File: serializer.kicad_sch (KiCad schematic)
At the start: 1 part

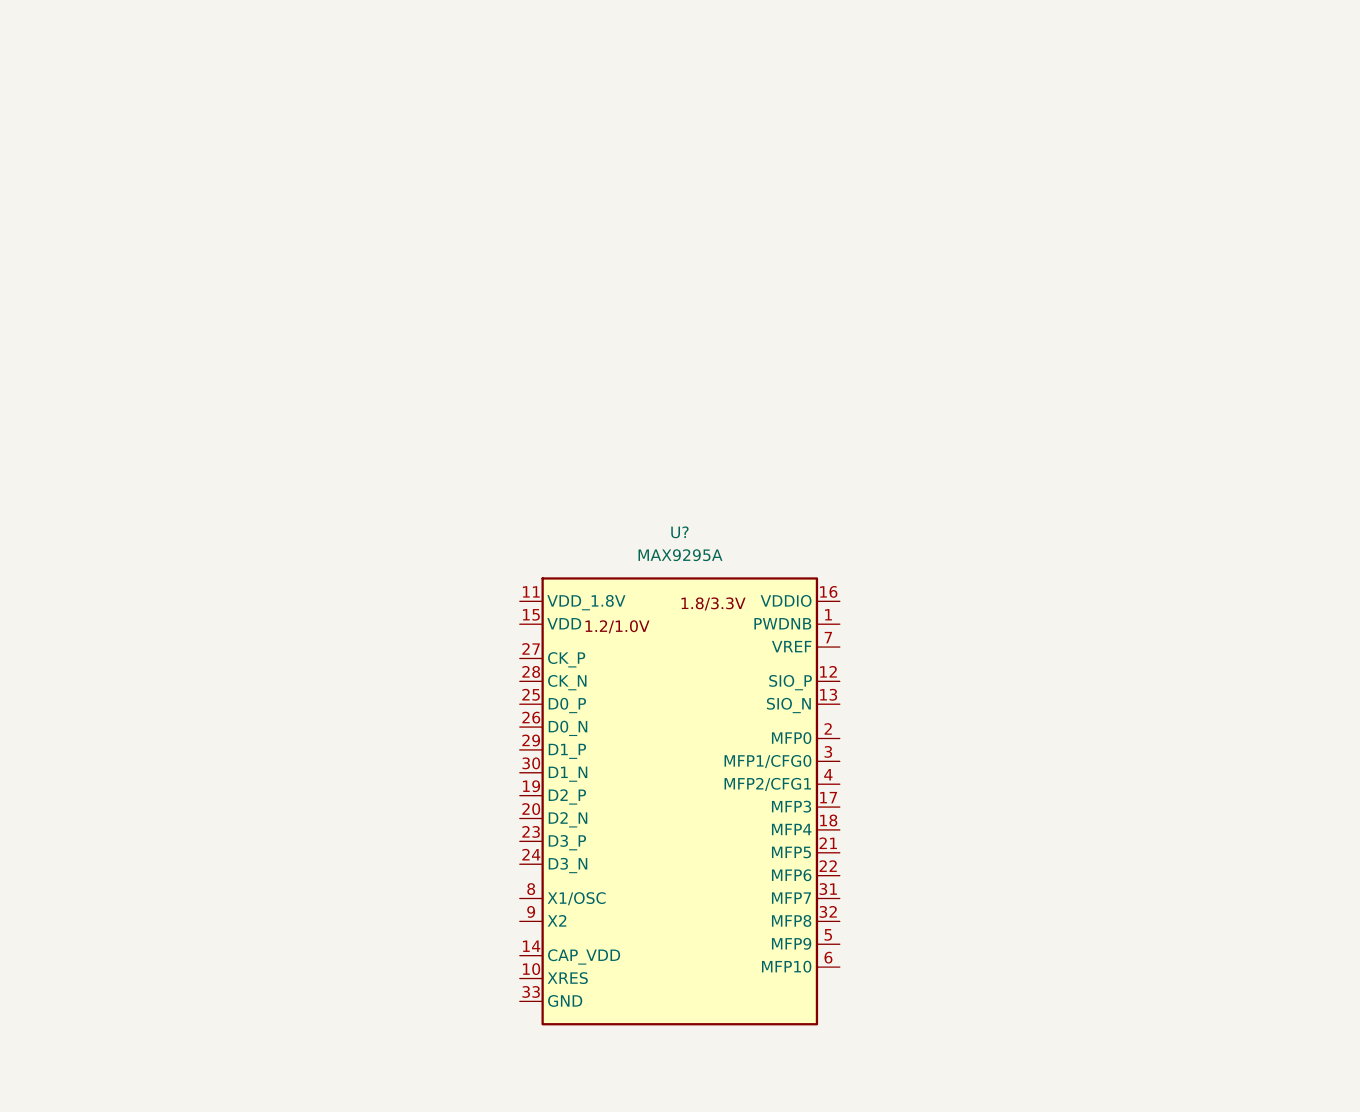
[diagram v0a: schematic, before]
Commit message: Add serializer supply filtration
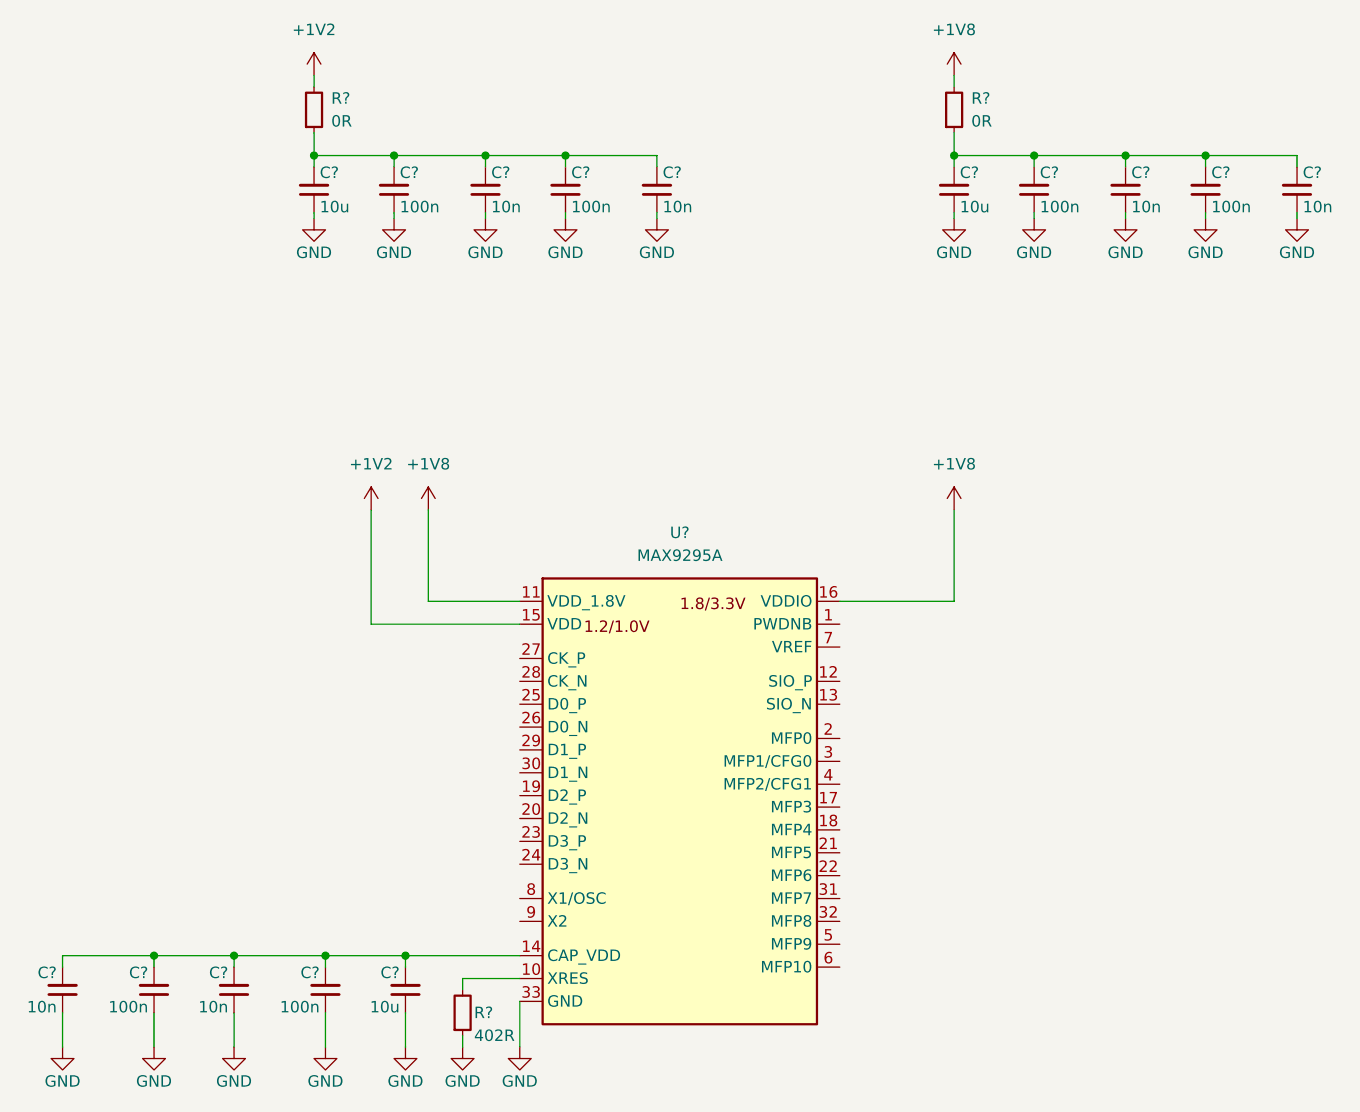
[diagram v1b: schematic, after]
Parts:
- added C? (x6): C_100n_0402, antmicro-footprints:C_0402_1005Metric, symbol antmicroCapacitors0402:C_100n_0402
- added C? (x6): C_10n_0402, antmicro-footprints:C_0402_1005Metric, symbol antmicroCapacitors0402:C_10n_0402
- added C? (x3): C_10u_0402, antmicro-footprints:C_0402_1005Metric, symbol antmicroCapacitors0402:C_10u_0402
- added R? (x2): R_0R_0402, antmicro-footprints:R_0402_1005Metric, symbol antmicroResistors0402:R_0R_0402
- added R?: R_402R_0402, antmicro-footprints:R_0402_1005Metric, symbol antmicroResistors0402:R_402R_0402
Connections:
- net at U?.10 (XRES): now also R?.2
- net +1V8: now reaches U?.11 (VDD_1.8V)
- net +1V8: now also U?.16 (VDDIO), R?.2
- net at U?.14 (CAP_VDD): now also C?.2, C?.2, C?.2, C?.2, C?.2
- net +1V2: now reaches U?.15 (VDD)
- net +1V2: now also R?.2
- net GND: now reaches U?.33 (GND)
- net GND: now also C?.1, C?.1, C?.1, C?.1, C?.1, C?.1, C?.1, C?.1, C?.1, C?.1, C?.1, C?.1, C?.1, C?.1, C?.1, R?.1
- new net: C?.2, C?.2, C?.2, C?.2, C?.2, R?.1 (x2)

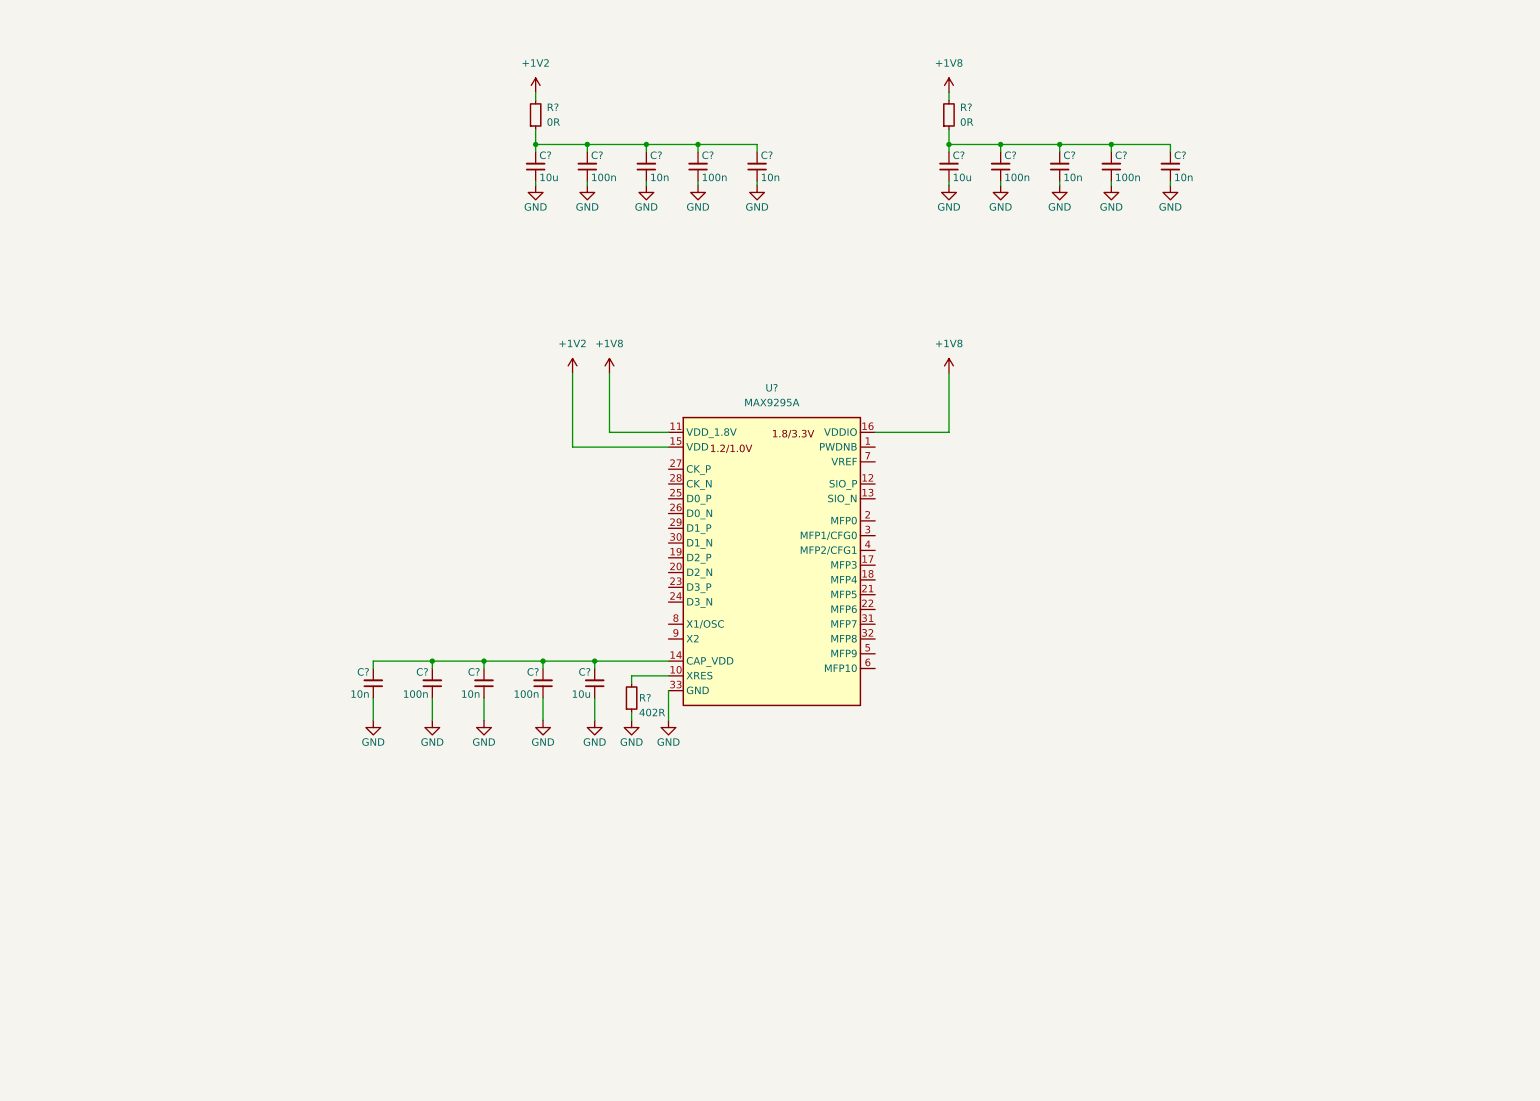
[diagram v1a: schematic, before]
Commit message: [WiP]:Add serializer signals and decoupling capacitors
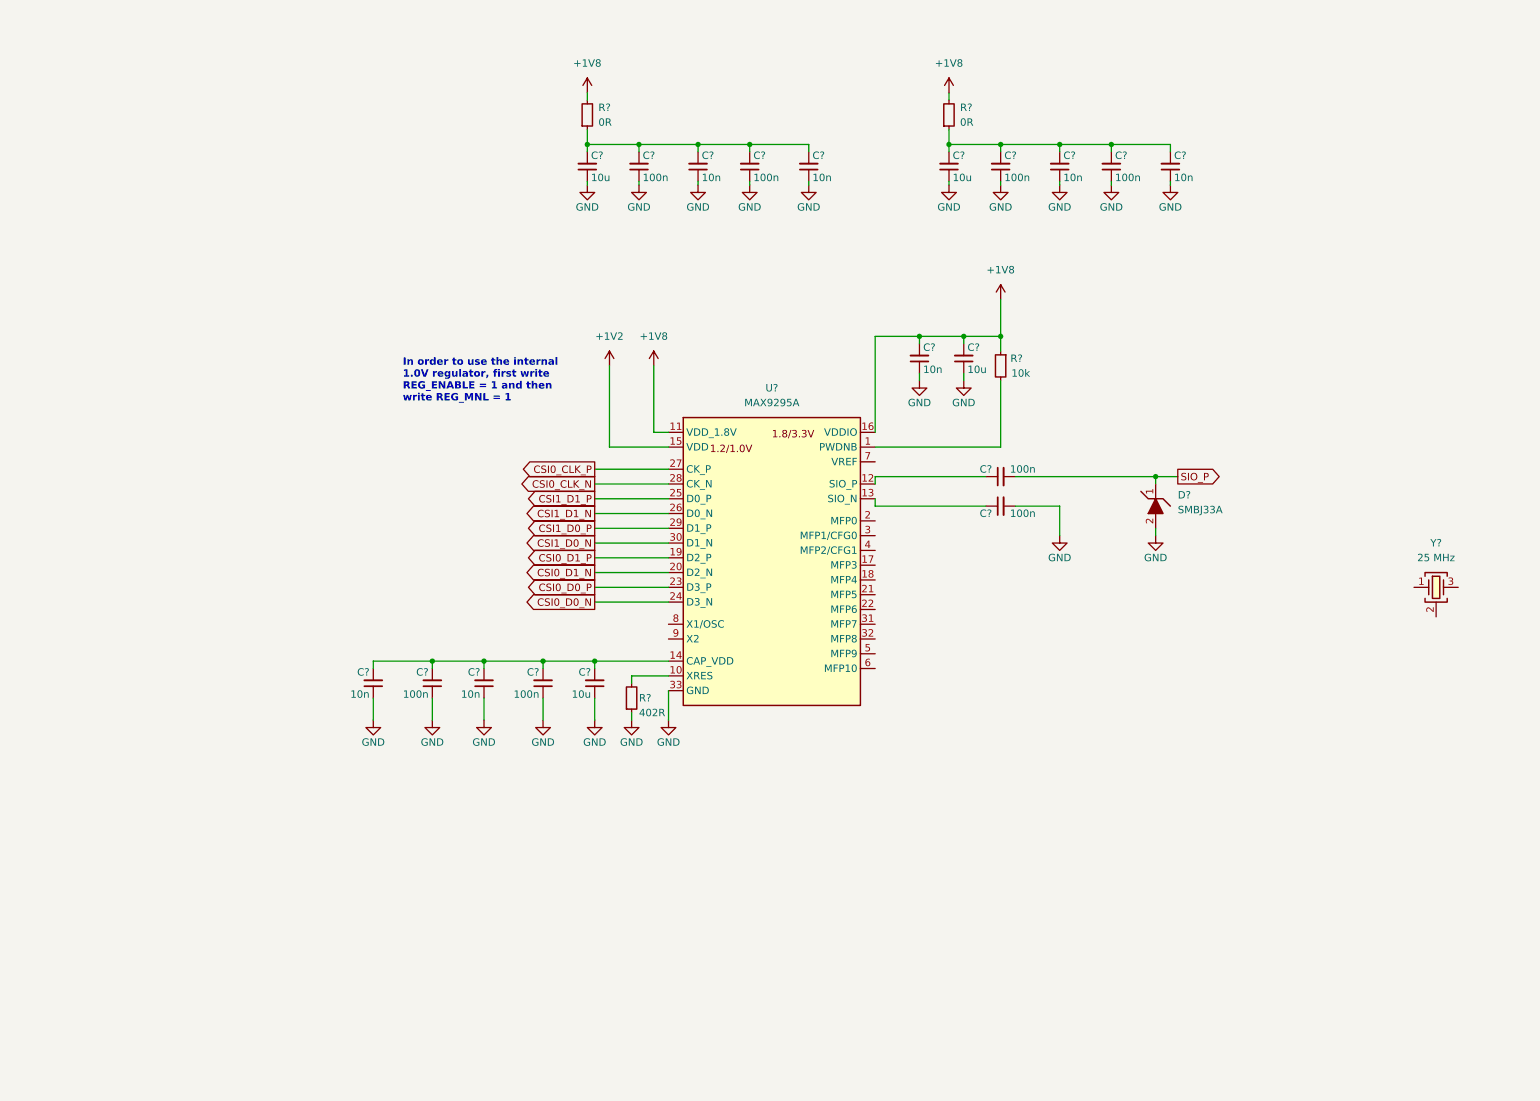
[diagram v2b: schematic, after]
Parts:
- removed C? (x2): C_10n_0402, antmicro-footprints:C_0402_1005Metric, symbol antmicroCapacitors0402:C_10n_0402
- removed C? (x2): C_100n_0402, antmicro-footprints:C_0402_1005Metric, symbol antmicroCapacitors0402:C_100n_0402
- removed C?: C_10u_0402, antmicro-footprints:C_0402_1005Metric, symbol antmicroCapacitors0402:C_10u_0402
- removed R?: R_0R_0402, antmicro-footprints:R_0402_1005Metric, symbol antmicroResistors0402:R_0R_0402
- added C? (x2): C_10u_0402, antmicro-footprints:C_0402_1005Metric, symbol antmicroCapacitors0402:C_10u_0402
- added C? (x4): C_100n_0402, antmicro-footprints:C_0402_1005Metric, symbol antmicroCapacitors0402:C_100n_0402
- added C? (x3): C_10n_0402, antmicro-footprints:C_0402_1005Metric, symbol antmicroCapacitors0402:C_10n_0402
- added D?: SMBJ33A, antmicro-footprints:D_SMB, symbol antmicroTVSDiodes:SMBJ33A
- added R?: R_0R_0402, antmicro-footprints:R_0402_1005Metric, symbol antmicroResistors0402:R_0R_0402
- added R?: R_10k_0402, antmicro-footprints:R_0402_1005Metric, symbol antmicroResistors0402:R_10k_0402
- added Y?: Resonator_25MHz_ABM8G, antmicro-footprints:Oscillator_SMD_Geyer_KX-7-4Pin_3.2x2.5mm, symbol antmicroResonators:Resonator_25MHz_ABM8G
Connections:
- net +1V8: now also C?.2, C?.2, R?.1, R?.2
- net GND: now also C?.1, C?.1, C?.1, C?.1, C?.1, C?.1, C?.1, C?.2, D?.2
- net at U?.1 (PWDNB): now also R?.2
- net at U?.12 (SIO_P): now also C?.1
- net at U?.13 (SIO_N): now also C?.1
- net CSI0_D1_P: now reaches U?.19 (D2_P)
- net CSI0_D1_N: now reaches U?.20 (D2_N)
- net CSI0_D0_P: now reaches U?.23 (D3_P)
- net CSI0_D0_N: now reaches U?.24 (D3_N)
- net CSI1_D1_P: now reaches U?.25 (D0_P)
- net CSI1_D1_N: now reaches U?.26 (D0_N)
- net CSI0_CLK_P: now reaches U?.27 (CK_P)
- net CSI0_CLK_N: now reaches U?.28 (CK_N)
- net CSI1_D0_P: now reaches U?.29 (D1_P)
- net CSI1_D0_N: now reaches U?.30 (D1_N)
- new net: C?.2, C?.2, C?.2, C?.2, C?.2, R?.1
- new net: Y?.2 (SH), Y?.4 (SH)
- new net SIO_P: C?.2, D?.1
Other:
- note added: "In order to use the internal 1.0V regulator, first write REG_ENABLE = 1 and then write REG_MNL = 1"

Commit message: Add cfg pins handling
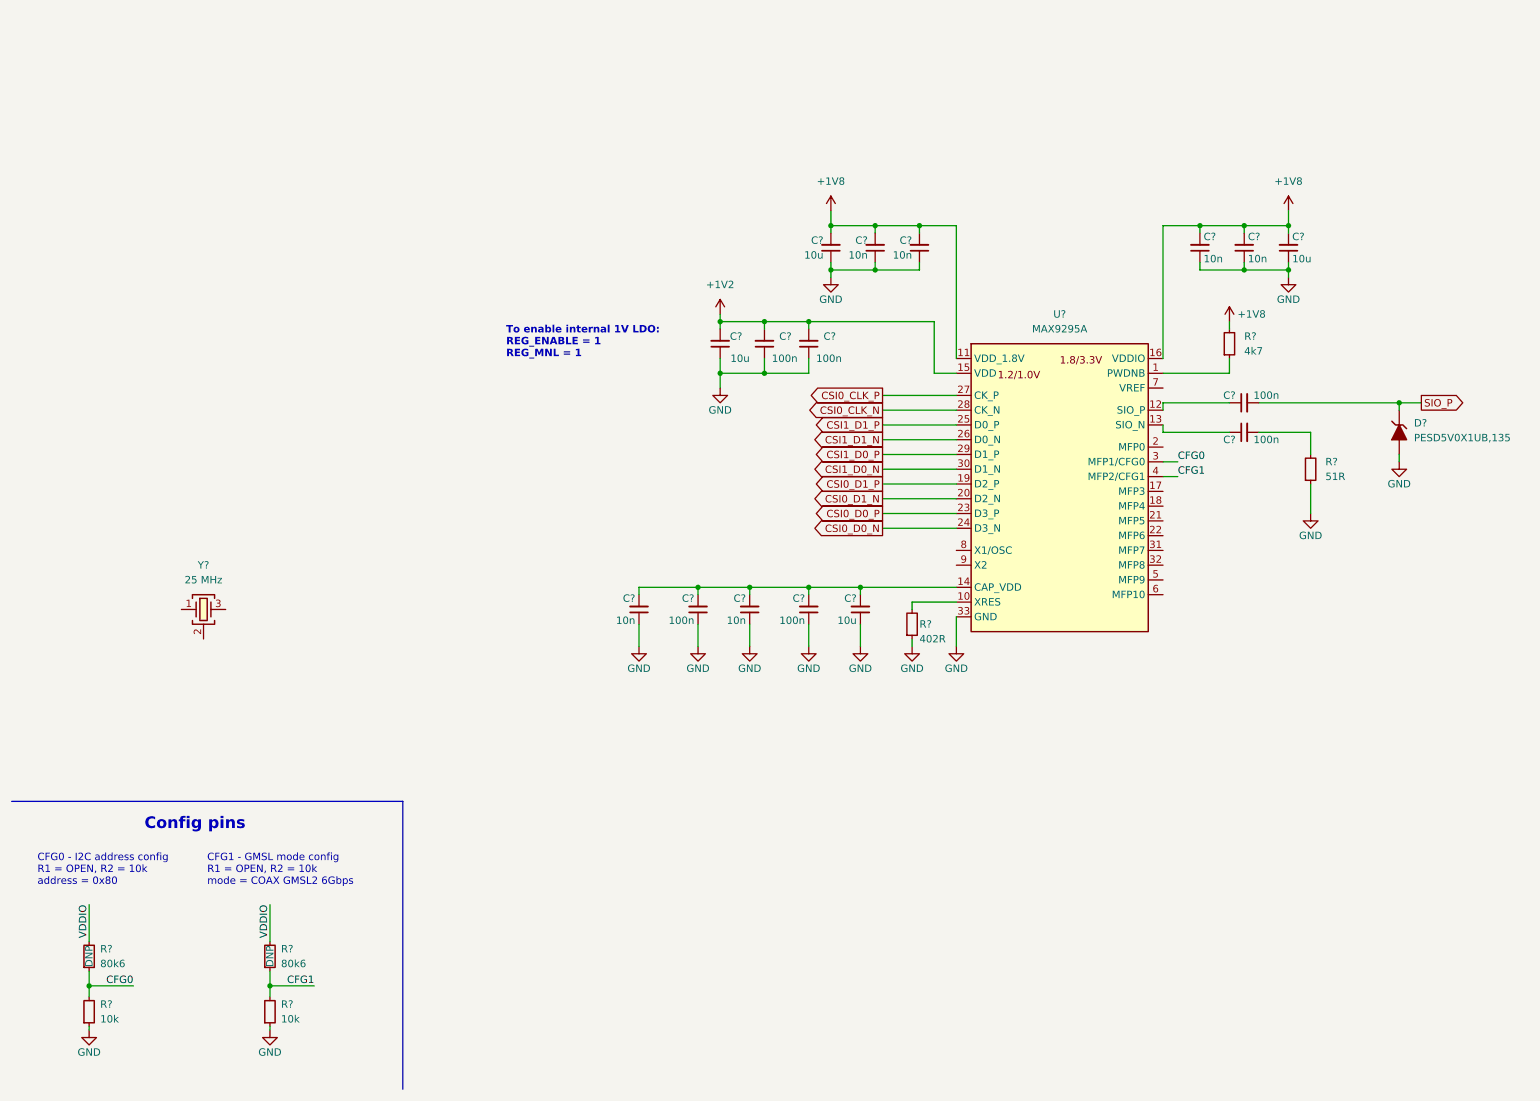
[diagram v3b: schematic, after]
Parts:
- removed C? (x2): C_10u_0402, antmicro-footprints:C_0402_1005Metric, symbol antmicroCapacitors0402:C_10u_0402
- removed C? (x4): C_10n_0402, antmicro-footprints:C_0402_1005Metric, symbol antmicroCapacitors0402:C_10n_0402
- removed C? (x4): C_100n_0402, antmicro-footprints:C_0402_1005Metric, symbol antmicroCapacitors0402:C_100n_0402
- removed D?: SMBJ33A, antmicro-footprints:D_SMB, symbol antmicroTVSDiodes:SMBJ33A
- removed R? (x2): R_0R_0402, antmicro-footprints:R_0402_1005Metric, symbol antmicroResistors0402:R_0R_0402
- removed R?: R_10k_0402, antmicro-footprints:R_0402_1005Metric, symbol antmicroResistors0402:R_10k_0402
- added C? (x2): C_10u_0402, antmicro-footprints:C_0402_1005Metric, symbol antmicroCapacitors0402:C_10u_0402
- added C? (x3): C_10n_0402, antmicro-footprints:C_0402_1005Metric, symbol antmicroCapacitors0402:C_10n_0402
- added C? (x2): C_100n_0402, antmicro-footprints:C_0402_1005Metric, symbol antmicroCapacitors0402:C_100n_0402
- added D?: PESD5V0X1UB, antmicro-footprints:SOD-523, symbol antmicroTVSDiodes:PESD5V0X1UB
- added R? (x2): R_80k6_0402, antmicro-footprints:R_0402_1005Metric, symbol antmicroResistors0402:R_80k6_0402
- added R?: R_4k7_0402, antmicro-footprints:R_0402_1005Metric, symbol antmicroResistors0402:R_4k7_0402
- added R?: R_51R_0402, antmicro-footprints:R_0402_1005Metric, symbol antmicroResistors0402:R_51R_0402
- added R? (x2): R_10k_0402, antmicro-footprints:R_0402_1005Metric, symbol antmicroResistors0402:R_10k_0402
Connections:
- net +1V2: now also C?.2, C?.2, C?.2
- net +1V8: now also C?.2, C?.2, C?.2, C?.2, R?.2
- net GND: now also C?.1, C?.1, C?.1, C?.1, C?.1, C?.1, C?.1, D?.2, R?.1, R?.1, R?.1; no longer C?.2
- net SIO_P: now also D?.1
- net at U?.1 (PWDNB): now also R?.1
- net CFG0: now reaches U?.3 (MFP1/CFG0)
- net CFG0: now also R?.1, R?.2
- net CFG1: now reaches U?.4 (MFP2/CFG1)
- net CFG1: now also R?.1, R?.2
- new net: C?.2, R?.2
- new net VDDIO: R?.2, R?.2
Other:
- note added: "CFG0 - I2C address config R1 = OPEN, R2 = 10k address = 0x80"
- note added: "CFG1 - GMSL mode config R1 = OPEN, R2 = 10k mode = COAX GMSL2 6Gbps"
- note added: "Config pins"
- note added: "To enable internal 1V LDO: REG_ENABLE = 1 REG_MNL = 1"
- note removed: "In order to use the internal 1.0V regulator, first write REG_ENABLE = 1 and then write REG_MNL = 1"
- moved on the sheet: C?, R?, U?, Y?
